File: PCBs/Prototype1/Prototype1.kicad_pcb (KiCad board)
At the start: 4 copper layers, 111.8 x 80.1 mm, 152 parts, among them J2 CMOD-A7, J3 PMOD, J4 2x20_Conn, Q1 2N7002NXAK, Q10 2N7002NXAK, Q11 2N7002NXAK, Q12 2N7002NXAK, Q13 2N7002NXAK, Q14 2N7002NXAK, Q15 2N7002NXAK, Q16 2N7002NXAK, Q17 2N7002NXAK, Q18 2N7002NXAK, Q2 2N7002NXAK, Q3 2N7002NXAK, Q4 2N7002NXAK, Q5 2N7002NXAK, Q6 2N7002NXAK, Q7 2N7002NXAK, Q8 2N7002NXAK, Q9 2N7002NXAK, U1 FXMAR2104UMX, U10 FXMAR2104UMX, U11 74LVC3G14, U12 FXMAR2104UMX, U2 FXMAR2104UMX, U3 FXMAR2104UMX, U4 FXMAR2104UMX, U5 FXMAR2104UMX, U6 FXMAR2104UMX, U7 74LVC3G14, U8 FXMAR2104UMX, U9 74LVC3G14

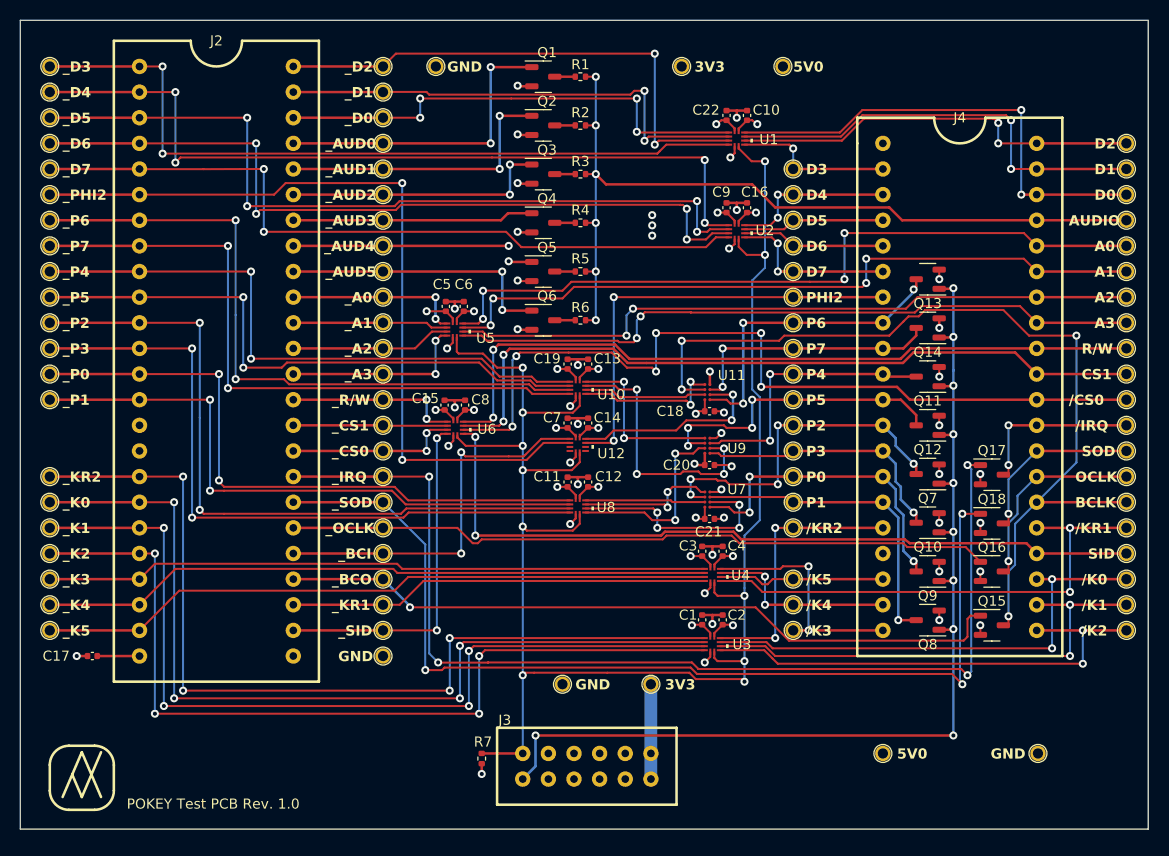
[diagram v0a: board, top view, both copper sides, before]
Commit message: Made prototype board and completed more verilog conversions
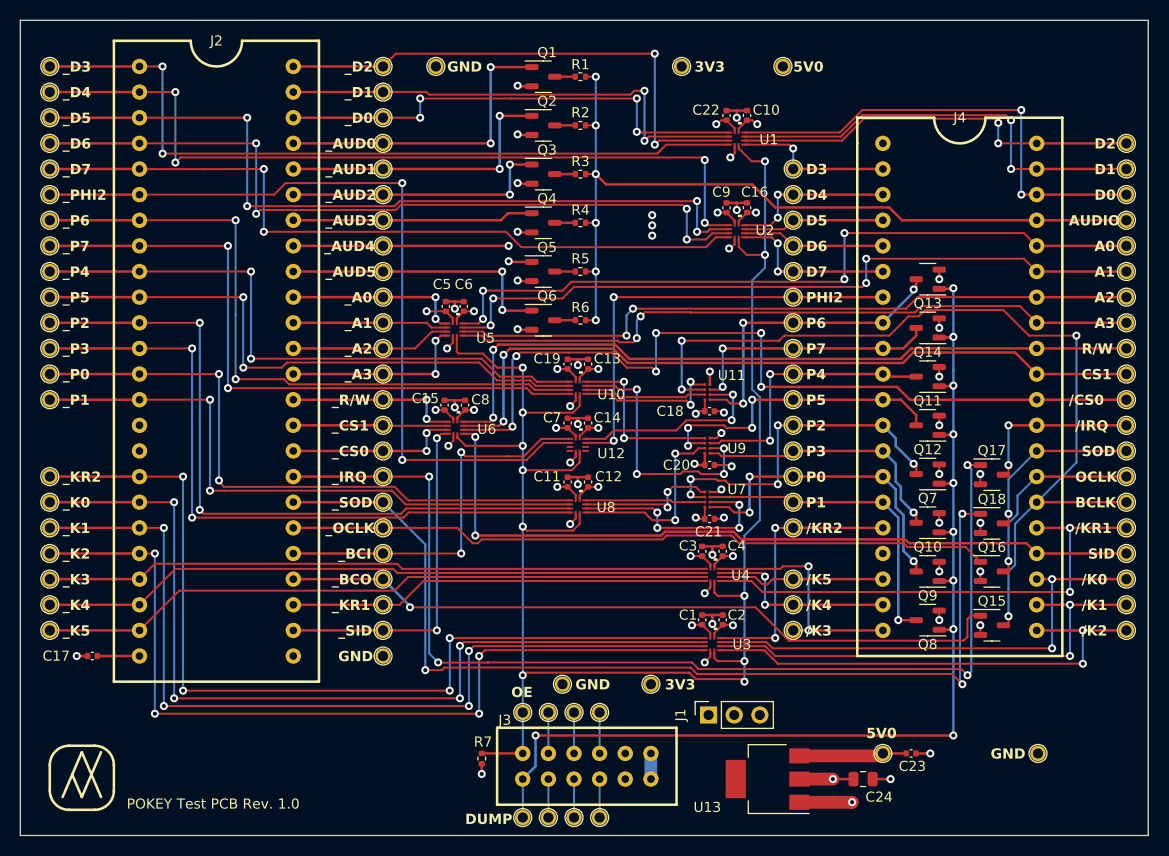
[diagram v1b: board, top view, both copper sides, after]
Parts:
- added C23: .1uf, Capacitor_SMD:C_0402_1005Metric, F.Cu at (190.8, 113.8)
- added C24: 10uf, Capacitor_SMD:C_0805_2012Metric, F.Cu at (186.0, 116.3)
- added J1: Conn_01x03_Pin, Connector_PinSocket_2.54mm:PinSocket_1x03_P2.54mm_Vertical, F.Cu at (170.7, 110.0)
- added TP91: ~, POKEY_Footprints:TP, F.Cu at (159.9, 109.7)
- added TP92: ~, POKEY_Footprints:TP, F.Cu at (157.4, 109.7)
- added TP93: ~, POKEY_Footprints:TP, F.Cu at (154.8, 109.7)
- added TP94: ~, POKEY_Footprints:TP, F.Cu at (154.8, 120.1)
- added TP95: ~, POKEY_Footprints:TP, F.Cu at (157.4, 120.1)
- added TP96: ~, POKEY_Footprints:TP, F.Cu at (159.9, 120.1)
- added TP97: ~, POKEY_Footprints:TP, F.Cu at (152.3, 120.1)
- added TP98: ~, POKEY_Footprints:TP, F.Cu at (152.3, 109.7)
- added U13: LD1117S33TR, POKEY_Footprints:Reg, F.Cu at (176.5, 116.1)
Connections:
- J3 pad 10: unconnected-(J3-JA10-Pad10) -> Net-(J3-JA10)
- J3 pad 12: +3.3V -> 3V3_A
- J3 pad 2: unconnected-(J3-JA2-Pad2) -> Net-(J3-JA2)
- J3 pad 3: unconnected-(J3-JA3-Pad3) -> Net-(J3-JA3)
- J3 pad 4: unconnected-(J3-JA4-Pad4) -> Net-(J3-JA4)
- J3 pad 6: +3.3V -> 3V3_A
- J3 pad 8: unconnected-(J3-JA8-Pad8) -> Net-(J3-JA8)
- J3 pad 9: unconnected-(J3-JA9-Pad9) -> Net-(J3-JA9)
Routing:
- net 3V3_B: track 0.00 -> 19.0 mm, vias 0 -> 1
- net 3V3_A: track 0.00 -> 12.1 mm
- net +5V: track 33.3 -> 44.0 mm
- net GND: track 66.6 -> 75.0 mm, vias 44 -> 47
- net Net-(J3-JA9): track 0.00 -> 4.06 mm
- net Net-(J3-JA8): track 0.00 -> 4.06 mm
- net Net-(J3-JA10): track 0.00 -> 4.06 mm
- net _DUMP: track 102.0 -> 105.8 mm
- net Net-(J3-JA4): track 0.00 -> 3.81 mm
- net Net-(J3-JA3): track 0.00 -> 3.81 mm
- net Net-(J3-JA2): track 0.00 -> 3.81 mm
- net +3.3V: track 186.0 -> 186.6 mm
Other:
- board size 111.8 x 80.1 mm -> 111.8 x 80.8 mm
- board text added: "DUMP"
- board text added: "OE"
